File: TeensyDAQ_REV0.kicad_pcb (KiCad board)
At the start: 2 copper layers, 101.6 x 82.6 mm, 99 parts, among them U100 TPS56637RPAR, U101 INA226AIDGSR, U102 BNO055, U103 SN65HVD230DR, U104 DRV5032FBDBZR, Y100 ABS07-32.768KHZ-T

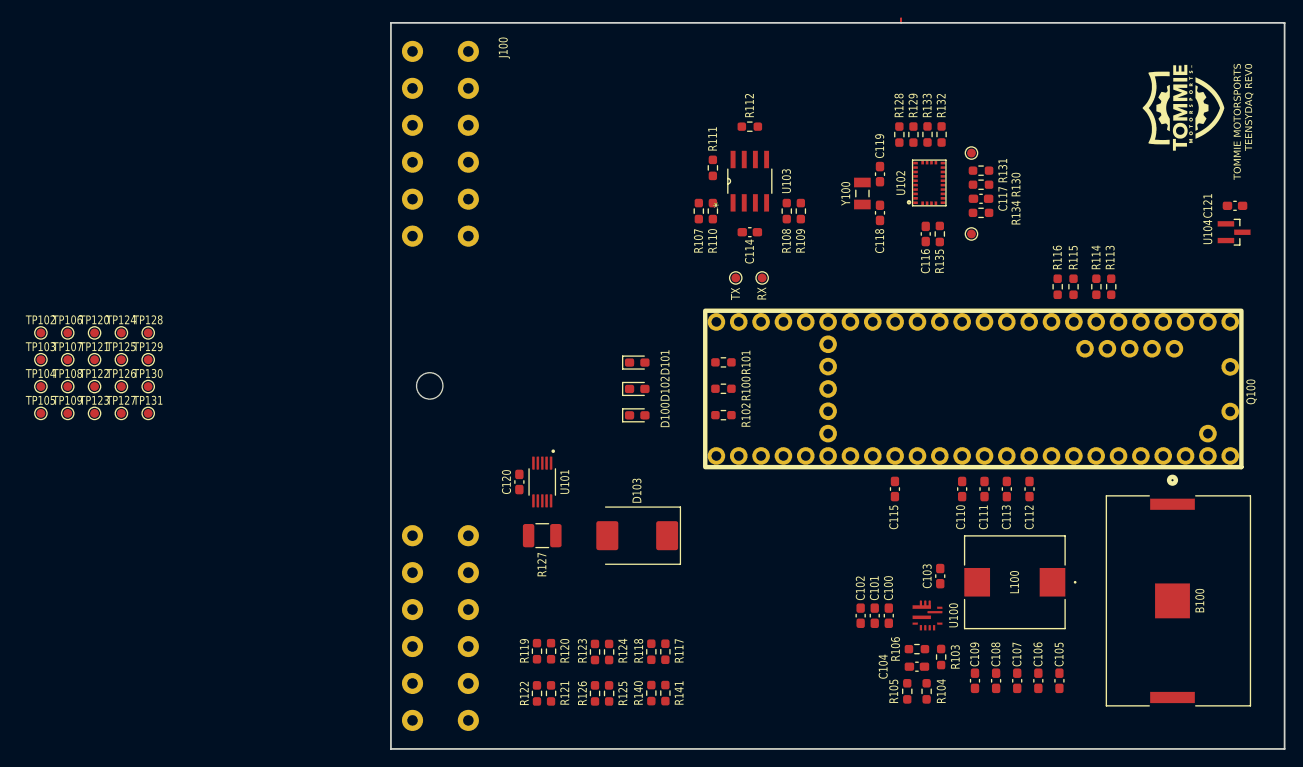
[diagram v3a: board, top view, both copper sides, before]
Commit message: final route. Needs revision and check of via placement.
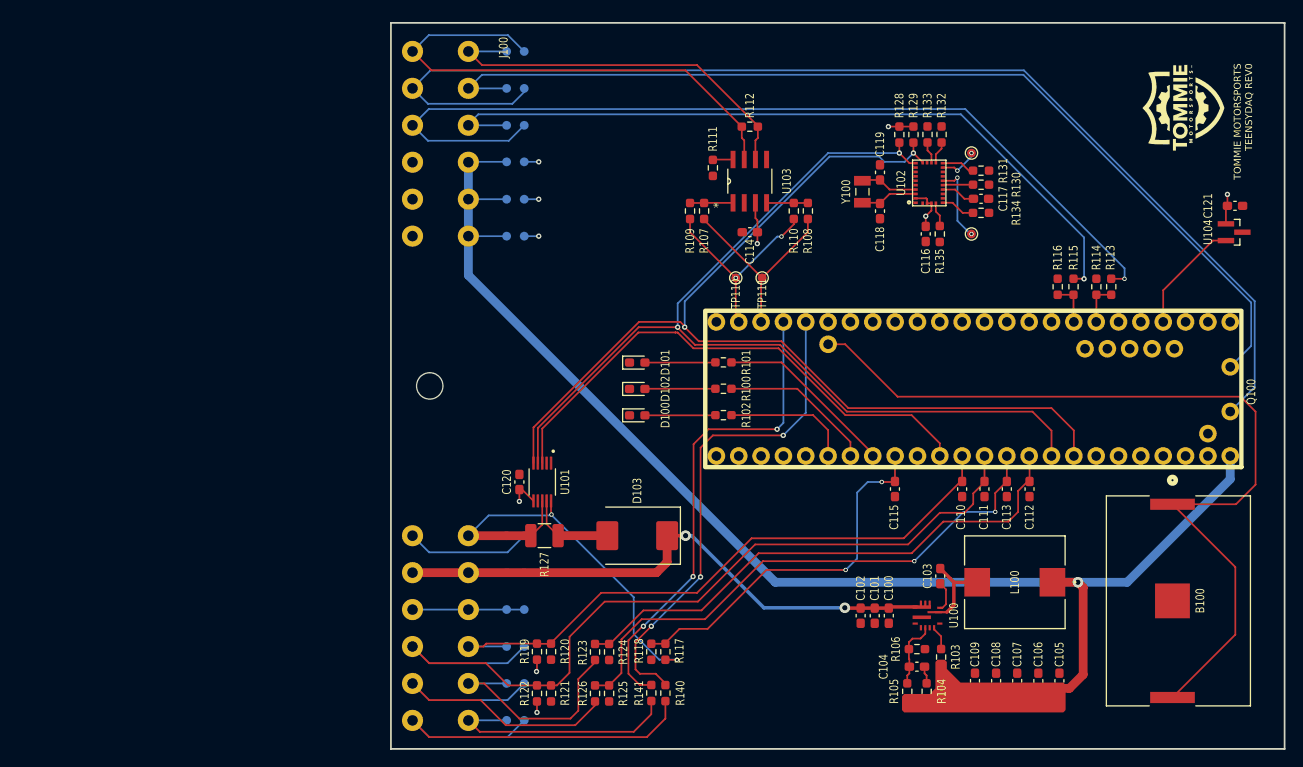
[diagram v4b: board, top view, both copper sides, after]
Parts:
- added 5V: TestPoint, TestPoint:TestPoint_Pad_D1.0mm, B.Cu at (113.2, 65.8)
- added 5V: TestPoint, TestPoint:TestPoint_Pad_D1.0mm, B.Cu at (113.2, 70.0)
- added G***: LOGO, qr:texas, B.Cu at (193.7, 123.6)
- added GND: TestPoint, TestPoint:TestPoint_Pad_D1.0mm, B.Cu at (115.2, 65.8)
- added GND: TestPoint, TestPoint:TestPoint_Pad_D1.0mm, B.Cu at (115.2, 70.0)
- added REF**: TestPoint_Pad_D1.5mm, TestPoint:TestPoint_Pad_D1.5mm, F.Cu at (164.6, 127.1)
- 5V: renamed from TP109; moved to B.Cu
- B+: renamed from TP120; moved to B.Cu
- CANH: renamed from TP105; moved to B.Cu
- CANL: renamed from TP106; moved to B.Cu
- C_T: renamed from TP128; moved to B.Cu
- D+: renamed from TP104; moved to B.Cu
- D-: renamed from TP107; moved to B.Cu
- E_T: renamed from TP123; moved to B.Cu
- GND: renamed from TP129; moved to B.Cu
- GND: renamed from TP131; moved to B.Cu
- GND: renamed from TP102; moved to B.Cu
- GND: renamed from TP122; moved to B.Cu
- HALL1: renamed from TP108; moved to B.Cu
- HALL2: renamed from TP103; moved to B.Cu
- I/O_1: renamed from TP125; moved to B.Cu
- I/O_2: renamed from TP126; moved to B.Cu
- P+: renamed from TP130; moved to B.Cu
- P+: renamed from TP121; moved to B.Cu
- VD_1: renamed from TP124; moved to B.Cu
- VD_2: renamed from TP127; moved to B.Cu
- moved CANH 68.7 mm to (115.2, 53.2), turned to 180 degrees
- moved D+ 62.9 mm to (113.2, 57.5), turned to 180 degrees
- moved HALL2 61.1 mm to (115.2, 61.6), turned to 180 degrees
- moved D- 60.4 mm to (115.2, 57.5), turned to 180 degrees
- moved I/O_1 60.0 mm to (113.2, 129.3), turned to 180 degrees
- moved I/O_2 59.5 mm to (115.2, 129.3), turned to 180 degrees
- moved CANL 59.3 mm to (113.2, 53.2), turned to 180 degrees
- moved VD_1 59.2 mm to (113.2, 125.1), turned to 180 degrees
- moved HALL1 58.1 mm to (113.2, 61.6), turned to 180 degrees
- moved GND 56.0 mm to (115.2, 74.2), turned to 180 degrees
- moved C_T 55.7 mm to (115.2, 120.9), turned to 180 degrees
- moved VD_2 55.1 mm to (115.2, 125.1), turned to 180 degrees
- moved E_T 53.8 mm to (113.2, 120.9), turned to 180 degrees
- moved 5V 53.8 mm to (113.2, 74.2), turned to 180 degrees
- moved P+ 52.7 mm to (113.2, 112.5), turned to 180 degrees
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- renumbered TX to TP110, RX to TP111
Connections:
- J100 pad 5: /Enclosure Connectors/USB_D+ -> /Enclosure Connectors/USB_D-
- J100 pad 8: /Enclosure Connectors/USB_D- -> /Enclosure Connectors/USB_D+
- Q100 pad 13: uLED -> /Power Biasing/INA226A_ALERT
- Q100 pad 2: unconnected-(Q100-Pad2) -> /Analog/Magnet_u
- Q100 pad 23: /Power Biasing/INA226A_ALERT -> unconnected-(Q100-Pad23)
- Q100 pad 32: /Analog/Magnet_u -> unconnected-(Q100-Pad32)
- Q100 pad 39: SD_LED -> uLED
- Q100 pad 40: unconnected-(Q100-Pad40) -> SD_LED
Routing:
- net +5V: track 0.00 -> 168.7 mm, vias 0 -> 1
- net /Enclosure Connectors/USB_D-: track 0.00 -> 135.6 mm
- net /Gyro/I2C_SCL: track 0.00 -> 117.7 mm, vias 0 -> 2
- net /Gyro/I2C_SDA: track 0.00 -> 113.4 mm, vias 0 -> 2
- net /Enclosure Connectors/USB_D+: track 0.00 -> 113.0 mm
- net /Analog/Hall_Signal1: track 0.00 -> 106.1 mm, vias 0 -> 1
- net RTC_BAT+: track 0.00 -> 98.3 mm
- net /Analog/CVT_Thermistor+: track 0.00 -> 96.8 mm
- net /Analog/Hall_Signal2: track 0.00 -> 86.6 mm, vias 0 -> 1
- net /Analog/Engine_Thermistor+: track 0.00 -> 71.3 mm
- net /Enclosure Connectors/Power_OUT+: track 0.00 -> 70.7 mm, vias 0 -> 2
- net /Analog/VDIV2_u: track 0.00 -> 62.8 mm, vias 0 -> 2
- net /Analog/VDIV1_u: track 0.00 -> 61.4 mm
- net /Power Biasing/INA226A_ALERT: track 0.00 -> 60.3 mm
- net /CAN/CANH: track 0.00 -> 59.1 mm
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- added copper zone on In2.Cu, net +3V3
- added copper zone on In1.Cu, net GND
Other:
- copper layers 2 -> 4

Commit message: added ground planes and 4 layer. Ran DRC and checked out
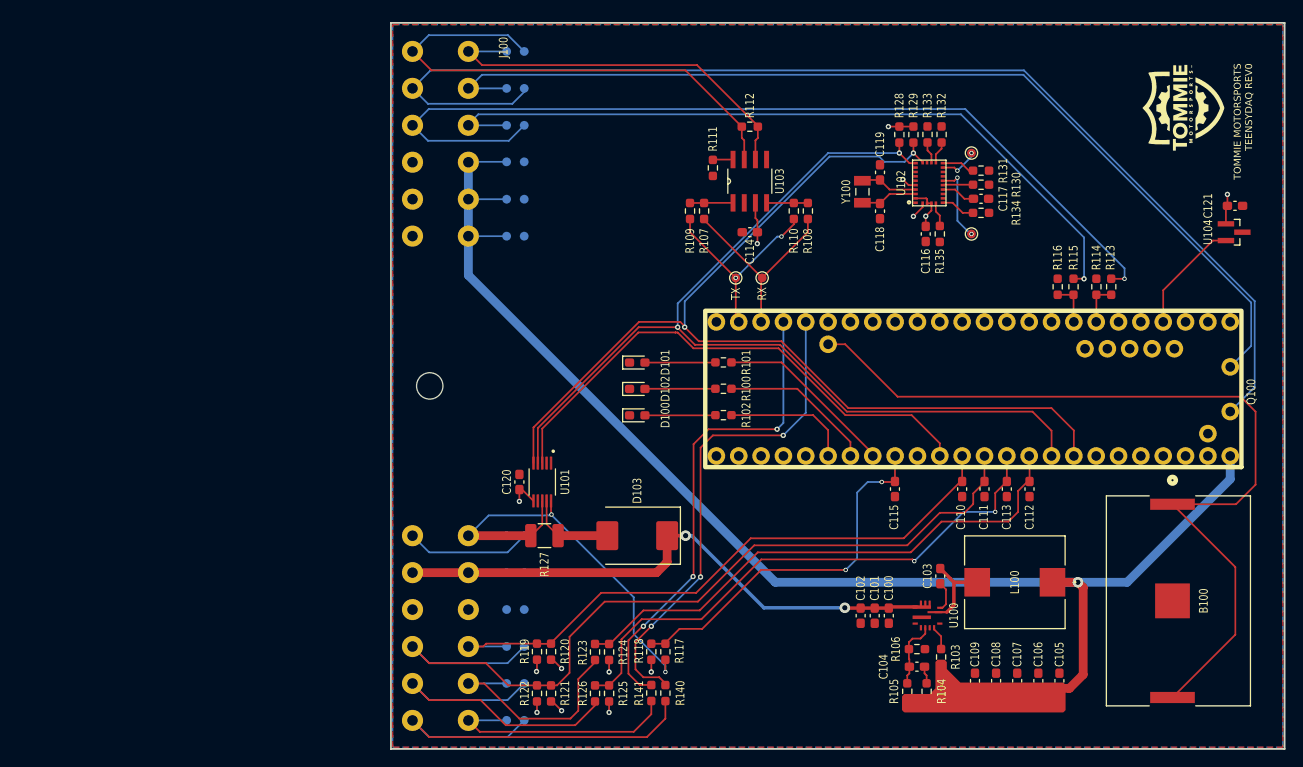
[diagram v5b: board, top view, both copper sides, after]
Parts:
- removed REF**: TestPoint_Pad_D1.5mm, TestPoint:TestPoint_Pad_D1.5mm
- renumbered TP111 to RX, TP110 to TX
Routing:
- net GND: track 31.9 -> 25.2 mm, vias 3 -> 7
- added copper zone on B.Cu, net GND
- added copper zone on F.Cu, net GND

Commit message: added more power tracks to power layer. re-ran fabrication output
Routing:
- net /Enclosure Connectors/Power_OUT+: track 70.7 -> 97.7 mm
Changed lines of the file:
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@@
+	)
+	(segment
+		(start 108.8 78.6)
+		(end 108.8 74.245)
+		(width 1)
+		(layer "In1.Cu")
+		(net 3)
 	)
 	(segment
 		(start 178.1 113.6)
-		(end 143.7 113.6)
-		(width 1)
-		(layer "B.Cu")
+		(end 143.8 113.6)
+		(width 1)
+		(layer "In1.Cu")
+		(net 3)
+	)
+	(segment
+		(start 108.8 70.045)
+		(end 108.8 65.845)
+		(width 1)
+		(layer "In1.Cu")
+		(net 3)
+	)
+	(segment
+		(start 143.8 113.6)
+		(end 108.8 78.6)
+		(width 1)
+		(layer "In1.Cu")
+		(net 3)
+	)
+	(segment
+		(start 108.8 74.245)
+		(end 108.8 70.045)
+		(width 1)
+		(layer "In1.Cu")
 		(net 3)
 	)
@@
 	)
 	(segment
-		(start 108.8 78.7)
-		(end 108.8 74.245)
-		(width 1)
-		(layer "B.Cu")
-		(net 3)
-	)
-	(segment
-		(start 108.8 74.245)
-		(end 108.8 70.045)
-		(width 1)
-		(layer "B.Cu")
-		(net 3)
-	)
-	(segment
 		(start 183.7 113.6)
 		(end 195.42 101.88)
@@
 	)
 	(segment
-		(start 108.8 70.045)
-		(end 108.8 65.845)
-		(width 1)
-		(layer "B.Cu")
-		(net 3)
-	)
-	(segment
 		(start 113.15 65.8)
 		(end 108.845 65.8)
@@
 	)
 	(segment
-		(start 143.7 113.6)
-		(end 108.8 78.7)
-		(width 1)
-		(layer "B.Cu")
-		(net 3)
-	)
-	(segment
 		(start 108.805 70.05)
 		(end 108.8 70.045)
@@
 		(end 159.825199 116.444265)
 		(width 0.2)
-		(layer "F.Cu")
-		(net 4)
-	)
-	(segment
-		(start 108.8 112.505)
-		(end 102.45 112.505)
-		(width 1)
 		(layer "F.Cu")
 		(net 4)
@@
 	)
 	(segment
+		(start 133.5 108.3)
+		(end 133.5 109.2)
+		(width 1)
+		(layer "In1.Cu")
+		(net 4)
+	)
+	(segment
+		(start 133.5 109.2)
+		(end 130.195 112.505)
+		(width 1)
+		(layer "In1.Cu")
+		(net 4)
+	)
+	(segment
+		(start 142.4 116.5)
+		(end 134.2 108.3)
+		(width 1)
+		(layer "In1.Cu")
+		(net 4)
+	)
+	(segment
+		(start 108.8 112.505)
+		(end 102.45 112.505)
+		(width 1)
+		(layer "In1.Cu")
+		(net 4)
+	)
+	(segment
+		(start 130.195 112.505)
+		(end 108.8 112.505)
+		(width 1)
+		(layer "In1.Cu")
+		(net 4)
+	)
+	(segment
+		(start 134.2 108.3)
+		(end 133.5 108.3)
+		(width 1)
+		(layer "In1.Cu")
+		(net 4)
+	)
+	(segment
+		(start 151.6 116.5)
+		(end 142.4 116.5)
+		(width 1)
+		(layer "In1.Cu")
+		(net 4)
+	)
+	(segment
 		(start 115.15 112.5)
 		(end 113.15 112.5)
@@
 	)
 	(segment
-		(start 142.4 116.5)
-		(end 151.6 116.5)
-		(width 0.4)
-		(layer "B.Cu")
-		(net 4)
-	)
-	(segment
-		(start 134.2 108.3)
-		(end 142.4 116.5)
-		(width 0.4)
-		(layer "B.Cu")
-		(net 4)
-	)
-	(segment
 		(start 113.15 112.5)
 		(end 108.805 112.5)
@@
 		(layer "B.Cu")
 		(net 4)
-	)
-	(segment
-		(start 133.5 108.3)
-		(end 134.2 108.3)
-		(width 0.4)
-		(layer "B.Cu")
-		(net 4)

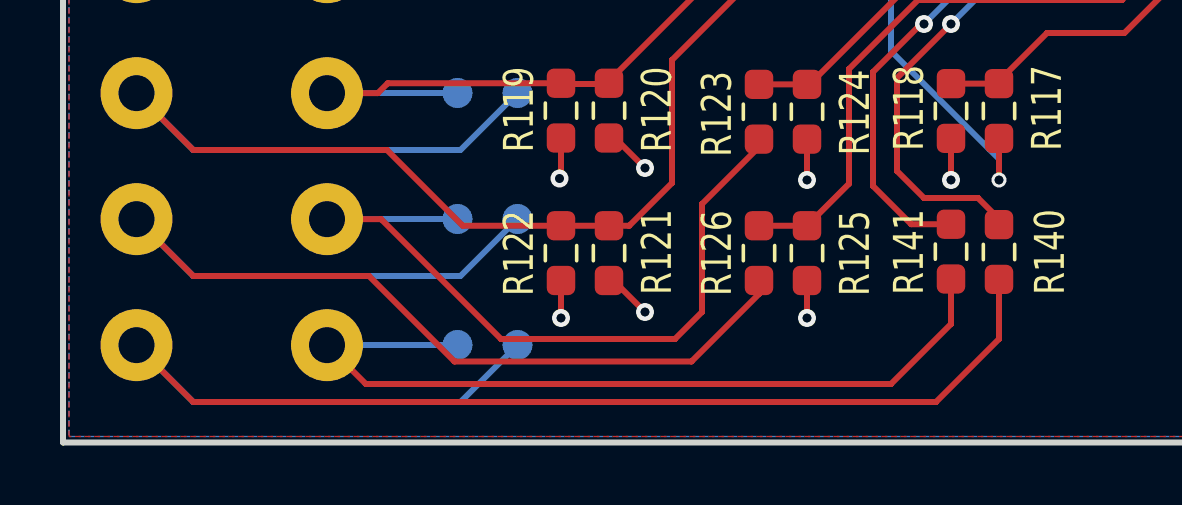
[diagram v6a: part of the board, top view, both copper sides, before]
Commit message: removed a VDIV input and changed it to a thermistor input. Re-ran fabrication output
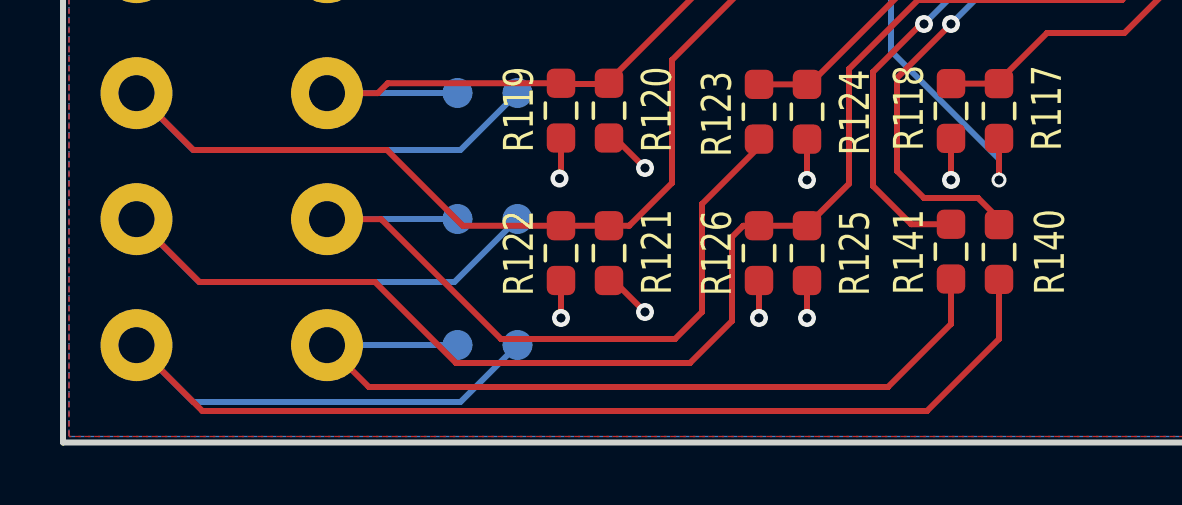
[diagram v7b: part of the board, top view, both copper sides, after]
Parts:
- renumbered VD_2 to 3_T, HALL2 to H1, HALL1 to H2
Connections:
- 3_T pad 1: /Analog/VDIV2+ -> /Analog/Thermistor3_u
- C113 pad 1: /Analog/VDIV2_u -> /Analog/Thermistor3_u
- J100 pad 20: /Analog/VDIV2+ -> /Analog/Thermistor3_u
- Q100 pad 16: /Analog/VDIV2_u -> /Analog/Thermistor3_u
- R125 pad 1: /Analog/VDIV2_u -> /Analog/Thermistor3_u
- R125 pad 2: /Analog/VDIV2+ -> +3V3
- R126 pad 2: /Analog/VDIV2_u -> /Analog/Thermistor3_u
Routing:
- net /Analog/Thermistor3_u: track 0.00 -> 103.7 mm, vias 0 -> 2
- net /Analog/VDIV2_u: track 63.0 -> 0.00 mm, vias 2 -> 0
- net /Analog/VDIV2+: track 38.4 -> 0.00 mm
- net +3V3: track 22.4 -> 23.7 mm, vias 7 -> 8
